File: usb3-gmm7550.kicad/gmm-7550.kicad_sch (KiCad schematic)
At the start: 35 parts, among them J4 10144517-061802LF, Q1 NX6008NBK, Q2 NX6008NBK, Q3 NX6008NBK, U6 SiP32510, U7 74LVC1G07, U8 INA180A2

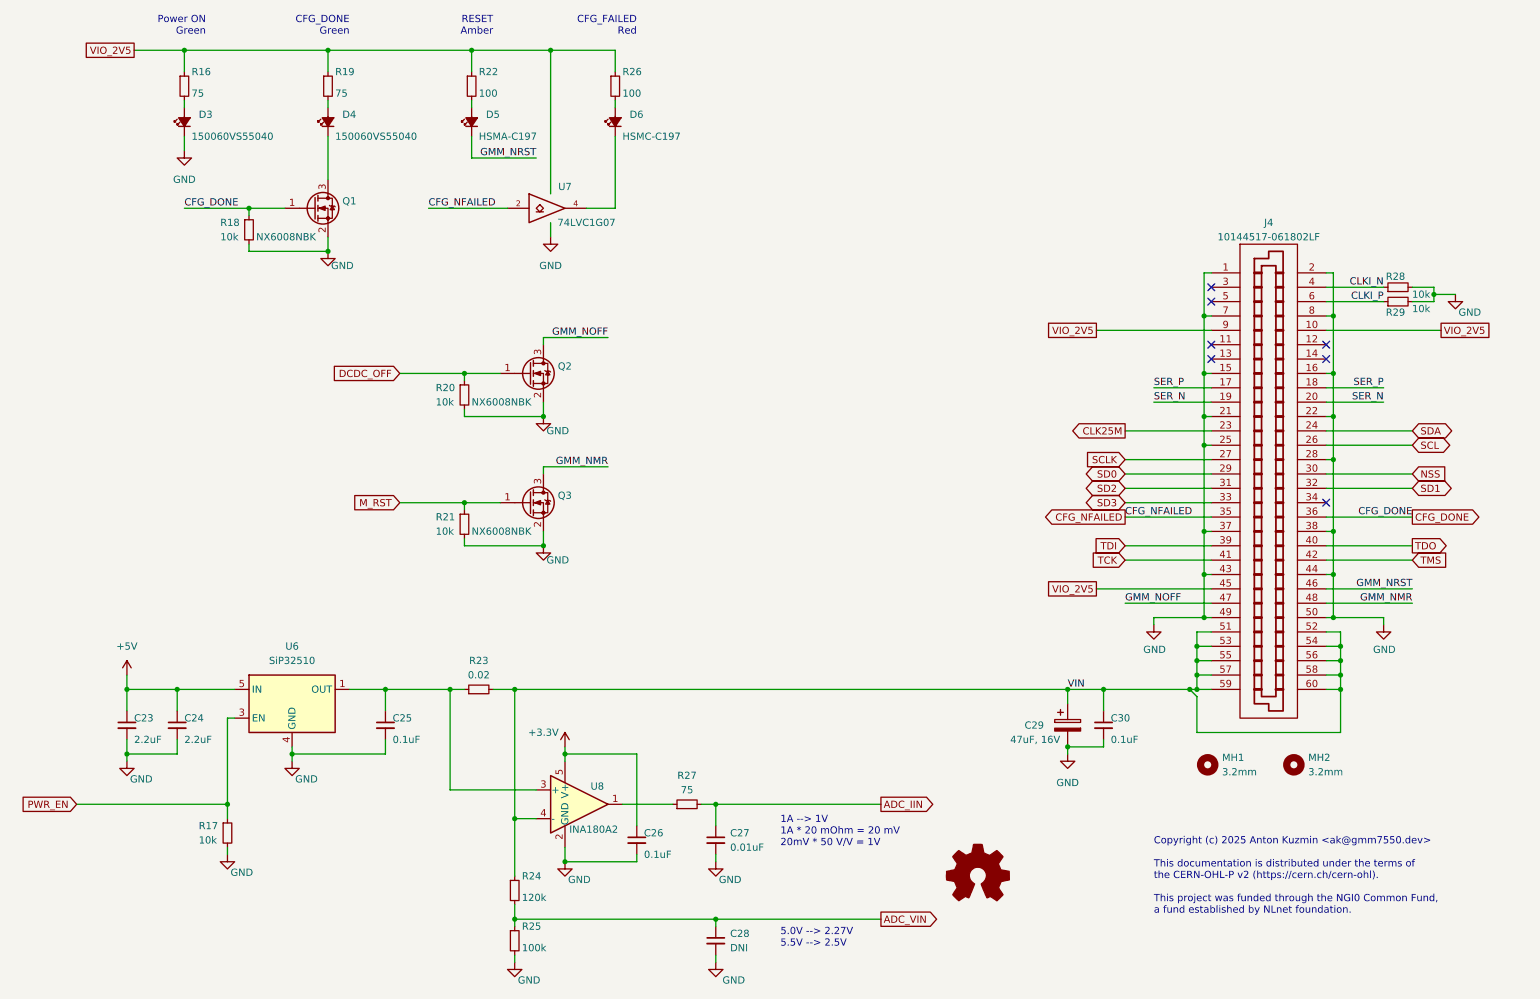
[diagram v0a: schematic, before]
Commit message: USB 3 adapter schematic -- WIP
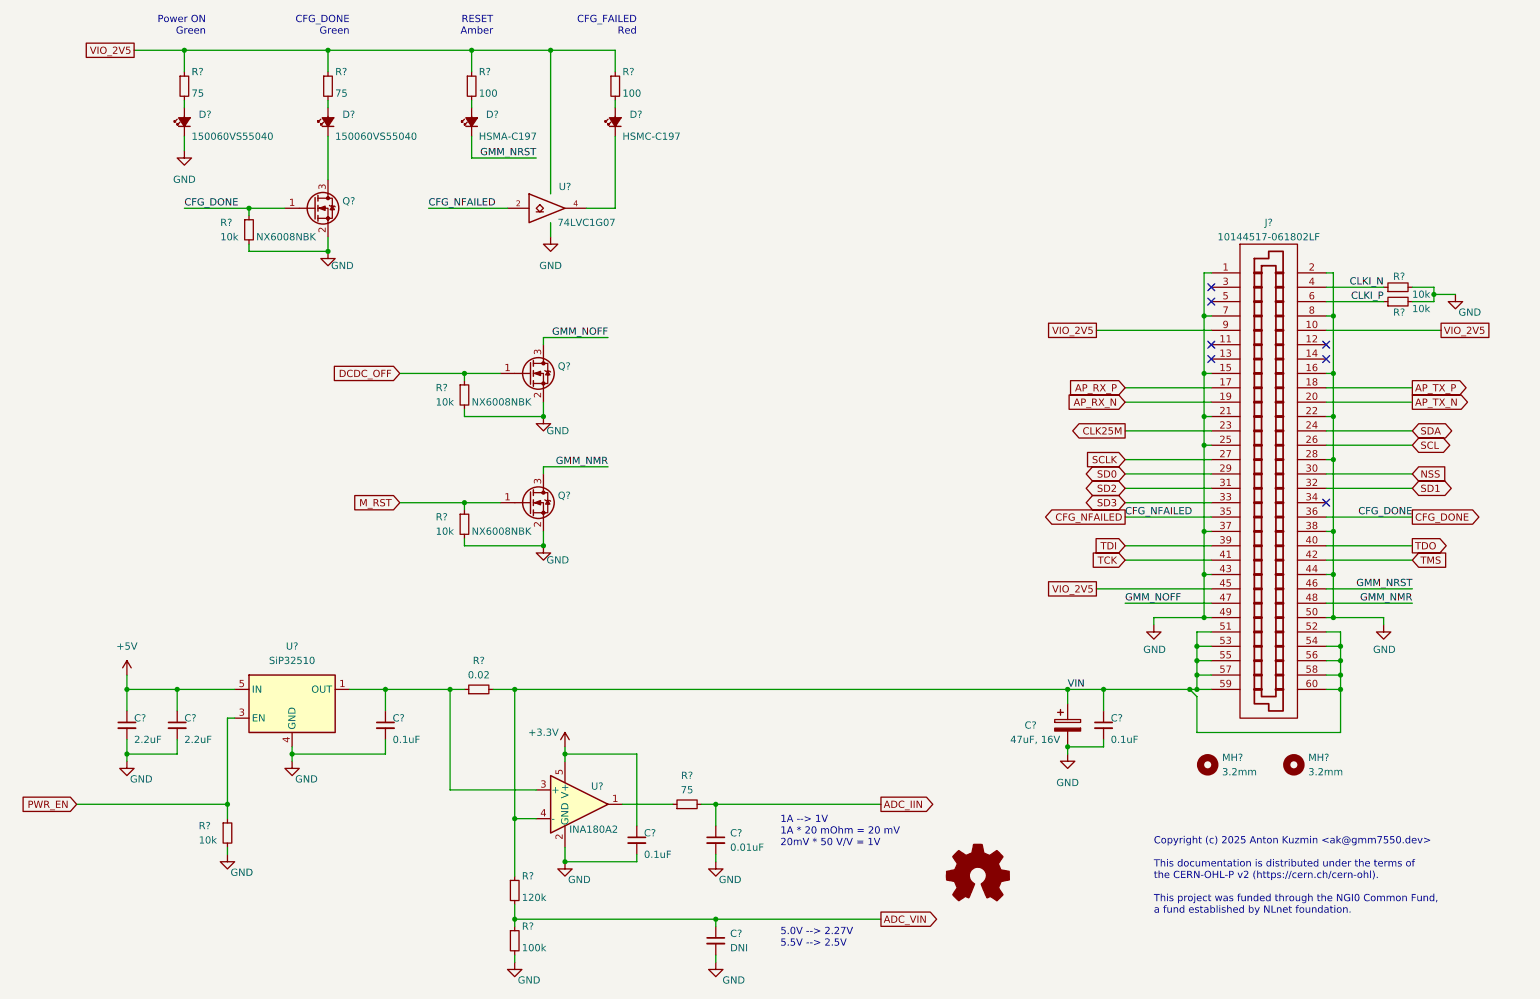
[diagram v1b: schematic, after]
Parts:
- renumbered C26 to C?, C29 to C?, C30 to C?, C24 to C?, C25 to C?, C27 to C?, C23 to C?, C28 to C?, D3 to D?, D5 to D?, D4 to D?, D6 to D?, J4 to J?, MH1 to MH?, MH2 to MH?, Q1 to Q?, Q3 to Q?, Q2 to Q?, R18 to R?, R16 to R?, R27 to R?, R24 to R?, R25 to R?, R29 to R?, R21 to R?, R19 to R?, R17 to R?, R26 to R?, R20 to R?, R28 to R?, R23 to R?, R22 to R?, U8 to U?, U7 to U?, U6 to U?
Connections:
- net SER_N renamed AP_RX_N
- net AP_RX_N: no longer J?.20
- net SER_P renamed AP_RX_P
- net AP_RX_P: no longer J?.18
- new net AP_TX_N: J?.20
- new net AP_TX_P: J?.18

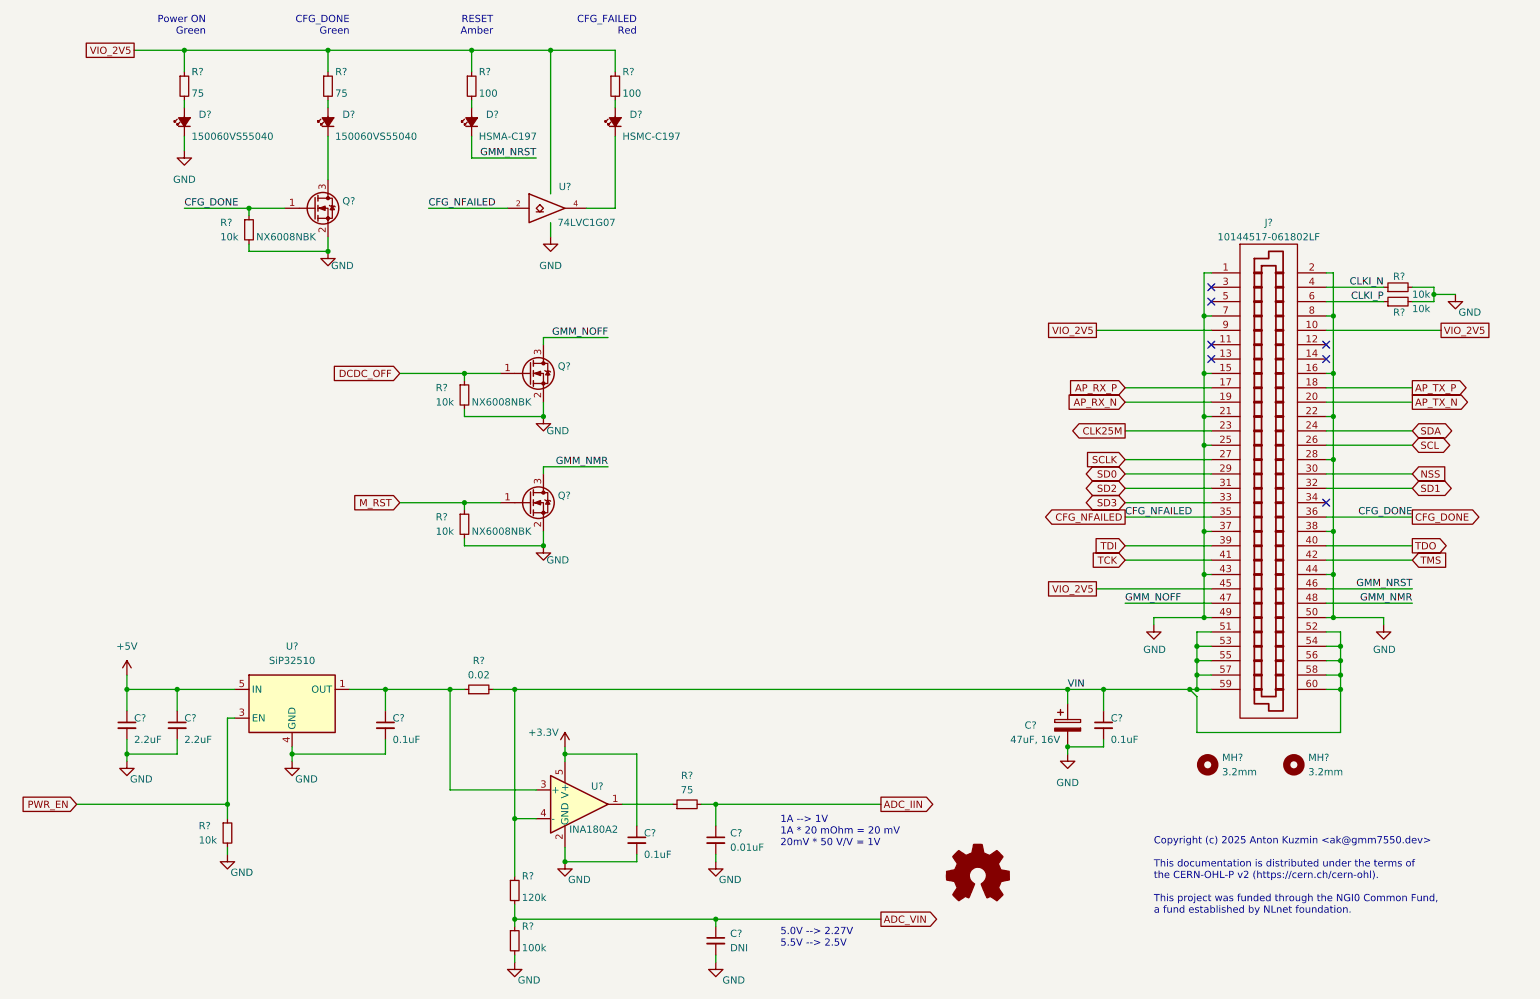
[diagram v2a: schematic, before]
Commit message: USB 3 adapter schematic -- WIP: USB 3 and Power Delivery pages
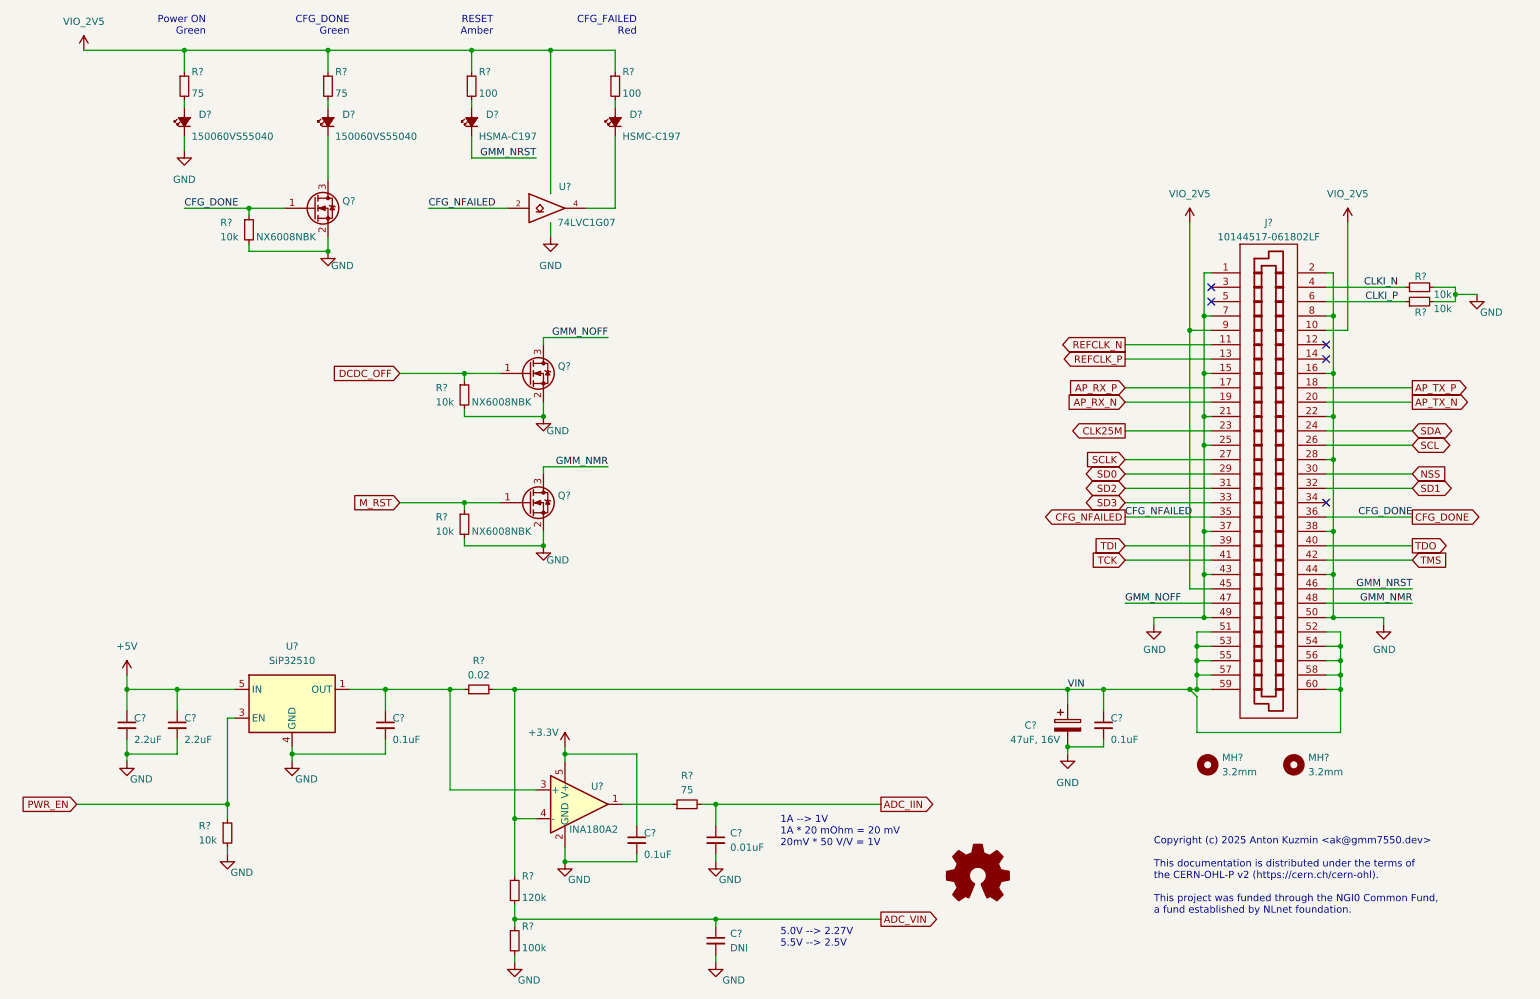
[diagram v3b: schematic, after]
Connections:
- net REFCLK_N: now reaches J?.11
- net REFCLK_P: now reaches J?.13
- no-connect marks 7 -> 5
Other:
- moved on the sheet: R?
